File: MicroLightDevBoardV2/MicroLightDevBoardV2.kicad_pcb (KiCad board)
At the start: 2 copper layers, 88.4 x 76.5 mm, 84 parts, among them J1 Conn_01x05_Socket, J10 Conn_01x02_Socket, J11 Conn_01x05_Socket, J12 Conn_01x02_Socket, J13 Conn_01x04_Socket, J14 Conn_01x04_Socket, J15 Conn_01x05_Socket, J16 Conn_01x02_Socket, J17 Conn_01x04_Socket, J18 Conn_01x02_Socket, J19 Conn_01x02_Socket, J2 Conn_01x05_Socket, J20 Conn_01x04_Socket, J21 Conn_01x04_Socket, J22 Conn_01x02_Socket, J23 Conn_01x02_Socket, J24 Conn_01x02_Socket, J25 Conn_01x02_Socket, J26 Conn_01x02_Socket, J27 Conn_01x04_Socket, J28 Conn_01x02_Socket, J29 Conn_01x04_Socket, J3 Conn_01x05_Socket, J30 Conn_01x04_Socket, J31 Conn_01x04_Socket, J32 Conn_01x04_Socket, J33 Conn_01x04_Socket, J34 Conn_01x04_Socket, J35 Conn_01x04_Socket, J36 Conn_01x04_Socket, J37 Conn_01x04_Socket, J38 Conn_01x04_Socket, J39 Conn_01x04_Socket, J4 Conn_01x05_Socket, J40 Conn_01x04_Socket, J41 Conn_01x04_Socket, J42 Conn_01x04_Socket, J43 Conn_01x04_Socket, J44 Conn_01x04_Socket, J45 Conn_01x04_Socket, J46 Conn_01x04_Socket, J47 Conn_01x04_Socket, J48 Conn_01x04_Socket, J49 Conn_01x04_Socket, J5 Conn_01x02_Socket, J50 Conn_01x04_Socket, J6 Conn_01x02_Socket, J7 TYPE-C-31-M-12, J8 Conn_01x02_Socket, J9 Conn_01x02_Socket, U1 BQ25628RYKR, U2 ATtiny3226-M, U3 S-85S1AB33-I6T1U, U4 B3U-1000P, U5 B3U-1000P, U6 USBLC6-2P6, U7 MC3479

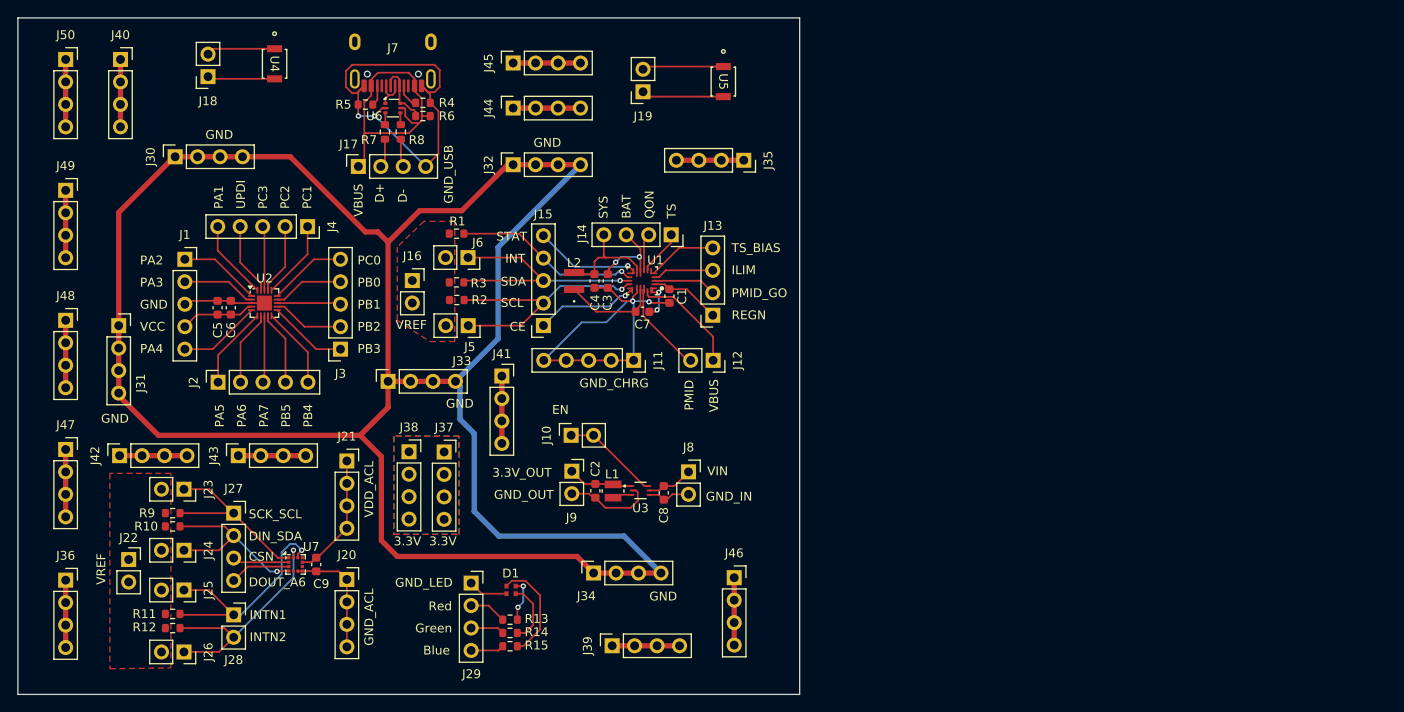
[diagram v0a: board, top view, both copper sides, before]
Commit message: organized new charger ic on pcb
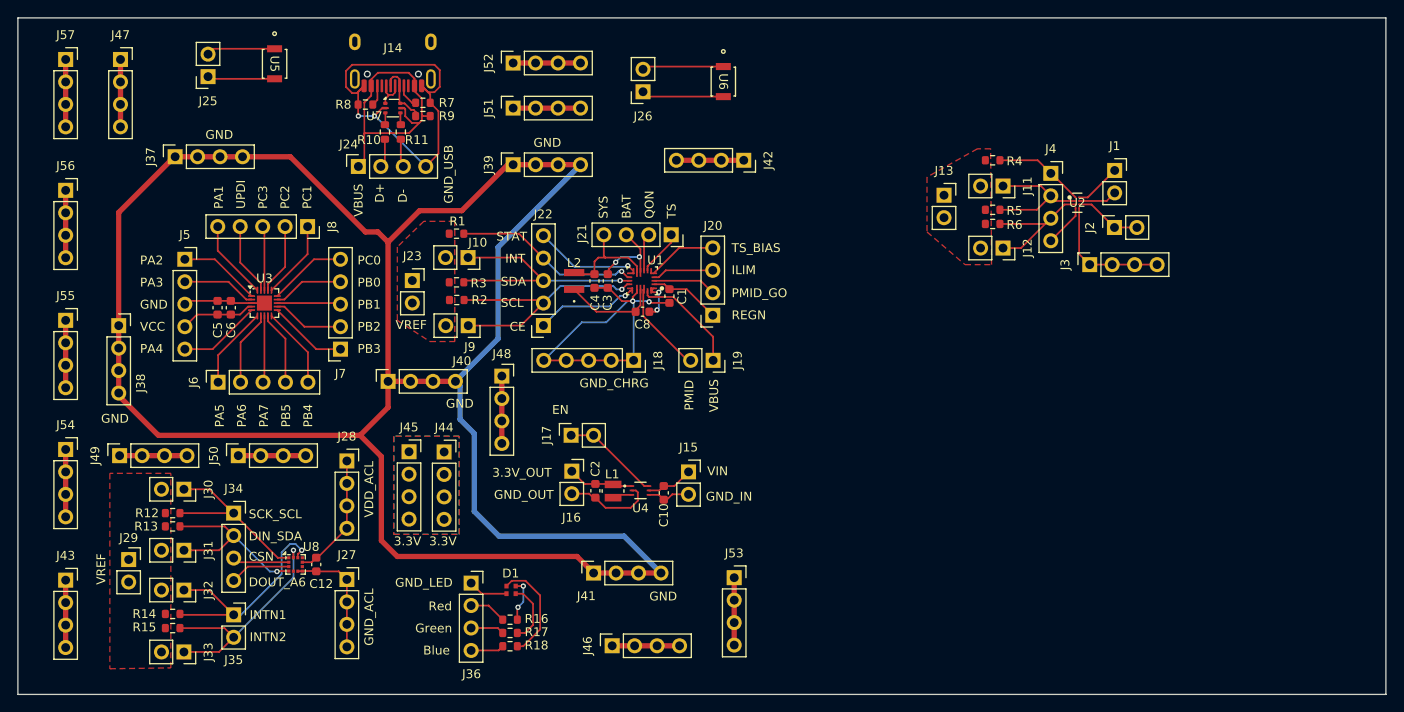
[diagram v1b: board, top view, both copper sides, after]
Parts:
- added J1: Conn_01x02_Socket, Connector_PinSocket_2.54mm:PinSocket_1x02_P2.54mm_Vertical, F.Cu at (235.3, 54.0)
- added J11: Conn_01x02_Socket, Connector_PinSocket_2.54mm:PinSocket_1x02_P2.54mm_Vertical, F.Cu at (222.7, 55.8)
- added J12: Conn_01x02_Socket, Connector_PinSocket_2.54mm:PinSocket_1x02_P2.54mm_Vertical, F.Cu at (222.7, 62.8)
- added J13: Conn_01x02_Socket, Connector_PinSocket_2.54mm:PinSocket_1x02_P2.54mm_Vertical, F.Cu at (216.0, 56.9)
- added J2: Conn_01x02_Socket, Connector_PinSocket_2.54mm:PinSocket_1x02_P2.54mm_Vertical, F.Cu at (235.3, 60.5)
- added J3: Conn_01x04_Socket, Connector_PinSocket_2.54mm:PinSocket_1x04_P2.54mm_Vertical, F.Cu at (232.5, 64.7)
- added J4: Conn_01x04_Socket, Connector_PinSocket_2.54mm:PinSocket_1x04_P2.54mm_Vertical, F.Cu at (228.1, 54.4)
- added R4: 10k, Resistor_SMD:R_0603_1608Metric, F.Cu at (221.5, 52.9)
- added R5: 10k, Resistor_SMD:R_0603_1608Metric, F.Cu at (221.5, 58.5)
- added R6: 10k, Resistor_SMD:R_0603_1608Metric, F.Cu at (221.5, 60.1)
- added U2: BQ25180, MicroLightDevBoard:BQ25180, F.Cu at (231.1, 57.7)
- renumbered C8 to C10, C9 to C12, C7 to C8, J6 to J10, J7 to J14, J8 to J15, J9 to J16, J10 to J17, J11 to J18, J12 to J19, J13 to J20, J14 to J21, J15 to J22, J16 to J23, J17 to J24, J18 to J25, J19 to J26, J20 to J27, J21 to J28, J22 to J29, J23 to J30, J24 to J31, J25 to J32, J26 to J33, J27 to J34, J28 to J35, J29 to J36, J30 to J37, J31 to J38, J32 to J39, J33 to J40, J34 to J41, J35 to J42, J36 to J43, J37 to J44, J38 to J45, J39 to J46, J40 to J47, J41 to J48, J42 to J49, J1 to J5, J43 to J50, J44 to J51, J45 to J52, J46 to J53, J47 to J54, J48 to J55, J49 to J56, J50 to J57, J2 to J6, J3 to J7, J4 to J8, J5 to J9, R7 to R10, R8 to R11, R9 to R12, R10 to R13, R11 to R14, R12 to R15, R13 to R16, R14 to R17, R15 to R18, R4 to R7, R5 to R8, R6 to R9, U2 to U3, U3 to U4, U4 to U5, U5 to U6, U6 to U7, U7 to U8
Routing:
- net SDA_CHG: track 0.00 -> 16.3 mm
- net SCL_CHG: track 0.00 -> 15.3 mm
- net GND_CHG: track 0.00 -> 14.5 mm
- net INT_CHG: track 0.00 -> 10.3 mm
- net BAT_CHG: track 0.00 -> 7.62 mm
- net VBUS_CHG: track 0.00 -> 5.29 mm
- net TS_MR_CHG: track 0.00 -> 4.86 mm
- net SYS_CHG: track 0.00 -> 4.40 mm
- added copper zone on F.Cu, net VREF_CHG
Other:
- board size 88.4 x 76.5 mm -> 154.7 x 76.5 mm

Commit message: integrated charger ic pcb breakout into the rest of the pcb
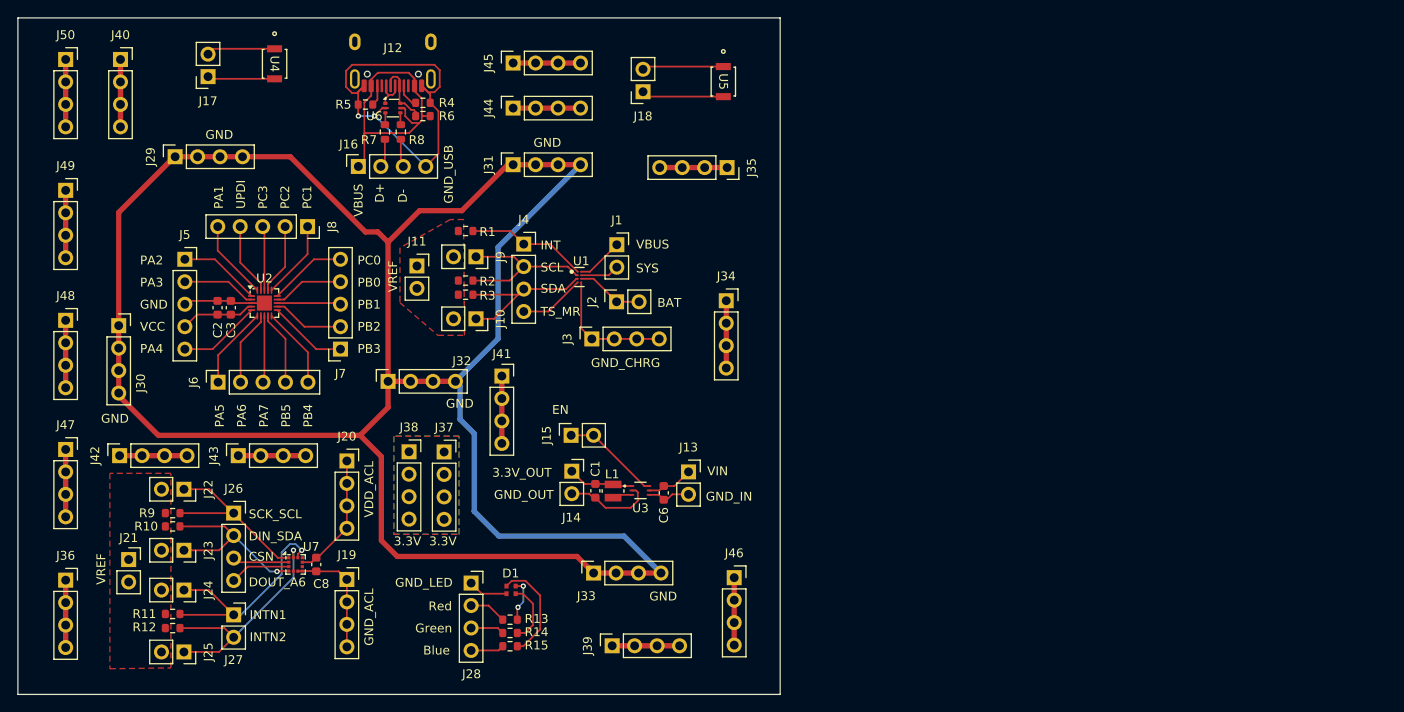
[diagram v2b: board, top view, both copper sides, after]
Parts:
- removed the C1 at (185.0, 68.2)
- removed the C3 at (178.0, 66.5)
- removed C4: 20uF, Capacitor_SMD:C_0603_1608Metric
- removed the C8 at (181.9, 70.0)
- removed the J10 at (162.2, 63.9)
- removed the J18 at (180.9, 75.5)
- removed the J19 at (189.9, 75.5)
- removed the J20 at (189.9, 70.4)
- removed the J21 at (185.2, 61.3)
- removed the J22 at (170.7, 71.6)
- removed the J23 at (155.9, 66.5)
- removed the J9 at (162.2, 71.6)
- removed L2: 1 uH, MicroLightDevBoard:74438322010_L
- removed the R1 at (160.9, 61.2)
- removed the R2 at (160.9, 68.7)
- removed the R3 at (160.9, 66.7)
- removed the U1 at (181.9, 66.5)
- added J34: Conn_01x04_Socket, Connector_PinSocket_2.54mm:PinSocket_1x04_P2.54mm_Vertical, F.Cu at (191.4, 68.8)
- moved J10 60.1 mm to (163.1, 70.8)
- moved J11 60.1 mm to (156.4, 64.8)
- moved J4 60.1 mm to (168.5, 62.4)
- moved J9 60.1 mm to (163.1, 63.8)
- moved R1 60.1 mm to (161.9, 60.9)
- moved R2 60.1 mm to (161.9, 66.5)
- moved R3 60.1 mm to (161.9, 68.1)
- moved J2 56.9 mm to (179.0, 68.9)
- moved J3 56.9 mm to (176.2, 73.1)
- moved J1 56.9 mm to (179.0, 62.4)
- moved U1 56.9 mm to (174.8, 66.1)
- moved J35 2.05 mm to (191.5, 53.7)
- renumbered C2 to C1, C5 to C2, C6 to C3, C10 to C6, C12 to C8, J12 to J10, J13 to J11, J14 to J12, J15 to J13, J16 to J14, J17 to J15, J24 to J16, J25 to J17, J26 to J18, J27 to J19, J28 to J20, J29 to J21, J30 to J22, J31 to J23, J32 to J24, J33 to J25, J34 to J26, J35 to J27, J36 to J28, J37 to J29, J38 to J30, J39 to J31, J40 to J32, J41 to J33, J42 to J35, J43 to J36, J44 to J37, J45 to J38, J46 to J39, J47 to J40, J48 to J41, J49 to J42, J50 to J43, J51 to J44, J52 to J45, J53 to J46, J54 to J47, J55 to J48, J56 to J49, J57 to J50, J11 to J9, R4 to R1, R13 to R10, R14 to R11, R15 to R12, R16 to R13, R17 to R14, R18 to R15, R5 to R2, R6 to R3, R7 to R4, R8 to R5, R9 to R6, R10 to R7, R11 to R8, R12 to R9, U2 to U1, U3 to U2, U4 to U3, U5 to U4, U6 to U5, U7 to U6, U8 to U7
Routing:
- net GND_CHRG: track 40.5 -> 0.00 mm, vias 2 -> 0
- net SCL_CHRG: track 29.6 -> 0.00 mm, vias 1 -> 0
- net SDA_CHRG: track 28.4 -> 0.00 mm, vias 1 -> 0
- net INT: track 21.1 -> 0.00 mm, vias 1 -> 0
- net SYS: track 12.7 -> 0.00 mm
- net VBUS_CHRG: track 12.5 -> 0.00 mm
- net STAT: track 11.9 -> 0.00 mm, vias 1 -> 0
- net CE: track 11.7 -> 0.00 mm, vias 1 -> 0
- net SW: track 10.8 -> 0.00 mm
- net PMID: track 10.5 -> 0.00 mm
- net BAT: track 9.63 -> 0.00 mm, vias 2 -> 0
- net REGN: track 8.06 -> 0.00 mm
- net TS_BIAS: track 7.87 -> 0.00 mm
- net Net-(J34-Pin_1): track 0.00 -> 7.62 mm
- net PMID_GO: track 7.18 -> 0.00 mm
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- removed copper zone on F.Cu, net VREF_CHRG
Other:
- board size 154.7 x 76.5 mm -> 86.2 x 76.5 mm
- board text added: "TS_MR"
- board text removed: "CE"
- board text removed: "ILIM"
- board text removed: "PMID"
- board text removed: "PMID_GO"
- board text removed: "QON"
- board text removed: "REGN"
- board text removed: "STAT"
- board text removed: "TS"
- board text removed: "TS_BIAS"

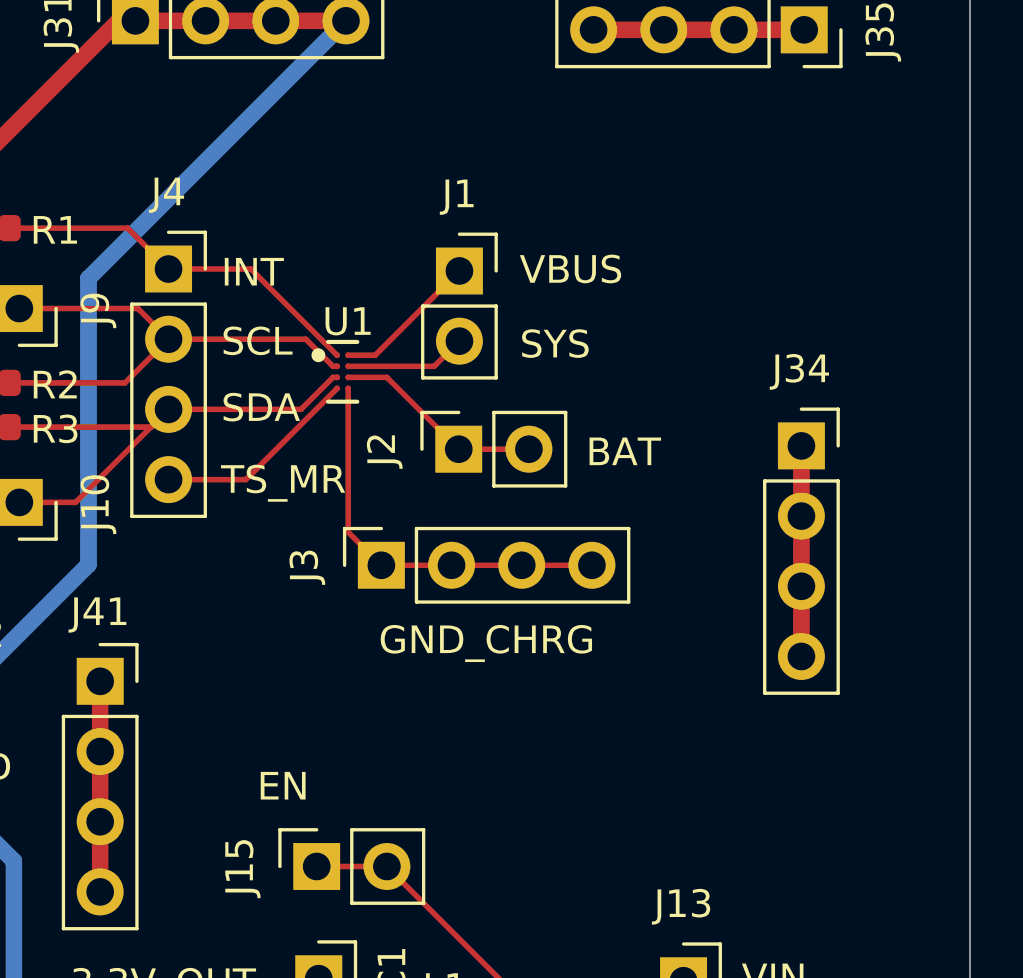
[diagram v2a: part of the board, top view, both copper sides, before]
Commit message: added missing capacitorson charging ic pcb
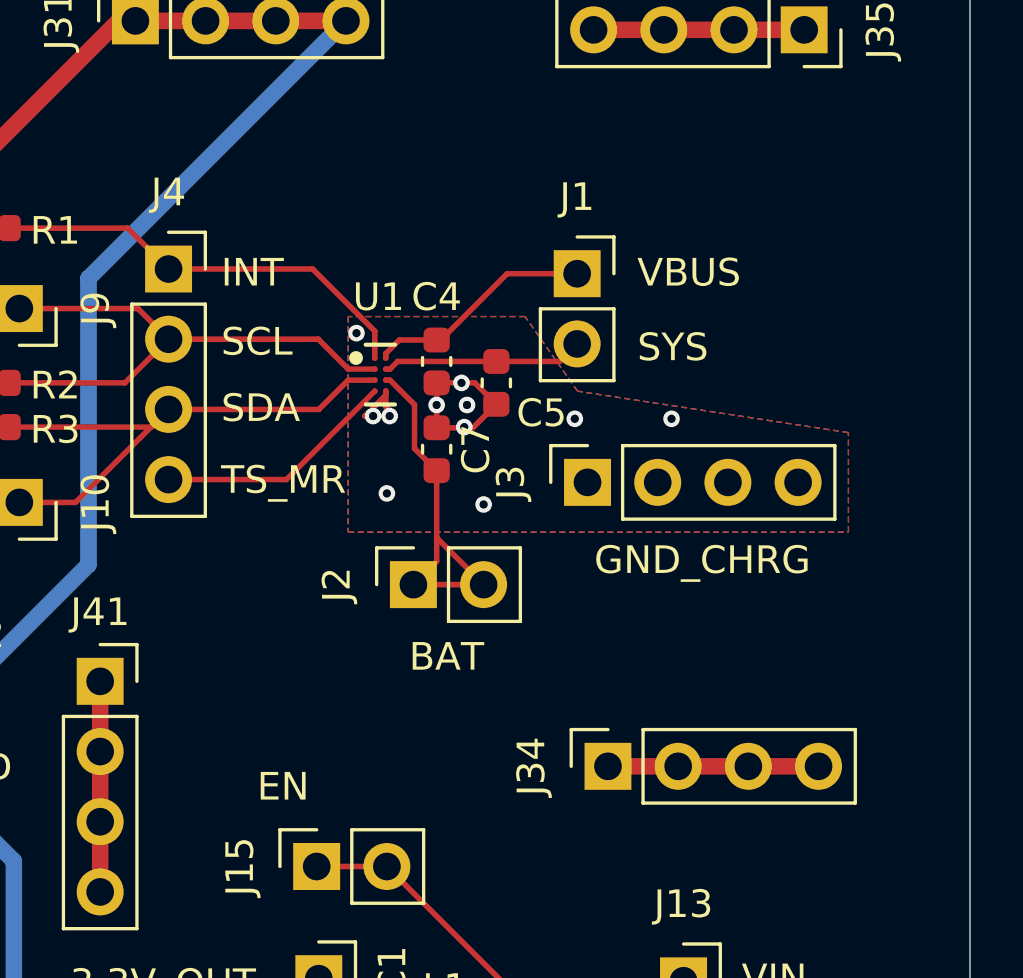
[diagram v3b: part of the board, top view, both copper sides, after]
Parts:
- added C4: C, Capacitor_SMD:C_0603_1608Metric, F.Cu at (178.2, 65.7)
- added C5: C, Capacitor_SMD:C_0603_1608Metric, F.Cu at (180.4, 66.5)
- added C7: C, Capacitor_SMD:C_0603_1608Metric, F.Cu at (178.2, 68.9)
- moved J34 13.5 mm to (184.4, 80.4), turned to 90 degrees
- moved J3 8.04 mm to (183.7, 70.1)
- moved J2 5.17 mm to (177.4, 73.8)
- moved J1 4.26 mm to (183.3, 62.5)
- moved U1 1.37 mm to (176.2, 66.2)
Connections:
- net BAT_CHG renamed BAT_CHRG
- net GND_CHG renamed GND_CHRG
- net INT_CHG renamed INT_CHRG
- net SCL_CHG renamed SCL_CHRG
- net SDA_CHG renamed SDA_CHRG
- net SYS_CHG renamed SYS_CHRG
- net TS_MR_CHG renamed TS_MR_CHRG
- net VBUS_CHG renamed VBUS_CHRG
- net VREF_CHG renamed VREF_CHRG
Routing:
- net BAT_CHRG: track 7.62 -> 13.5 mm
- net GND_CHRG: track 14.5 -> 9.45 mm, vias 0 -> 11
- net VBUS_CHRG: track 5.29 -> 8.28 mm
- net SYS_CHRG: track 4.40 -> 7.30 mm
- net INT_CHRG: track 13.8 -> 15.7 mm
- net SCL_CHRG: track 18.8 -> 20.2 mm
- net TS_MR_CHRG: track 7.47 -> 8.79 mm
- net SDA_CHRG: track 19.4 -> 20.7 mm
- added copper zone on B.Cu, net GND_CHRG
- added copper zone on F.Cu, net GND_CHRG

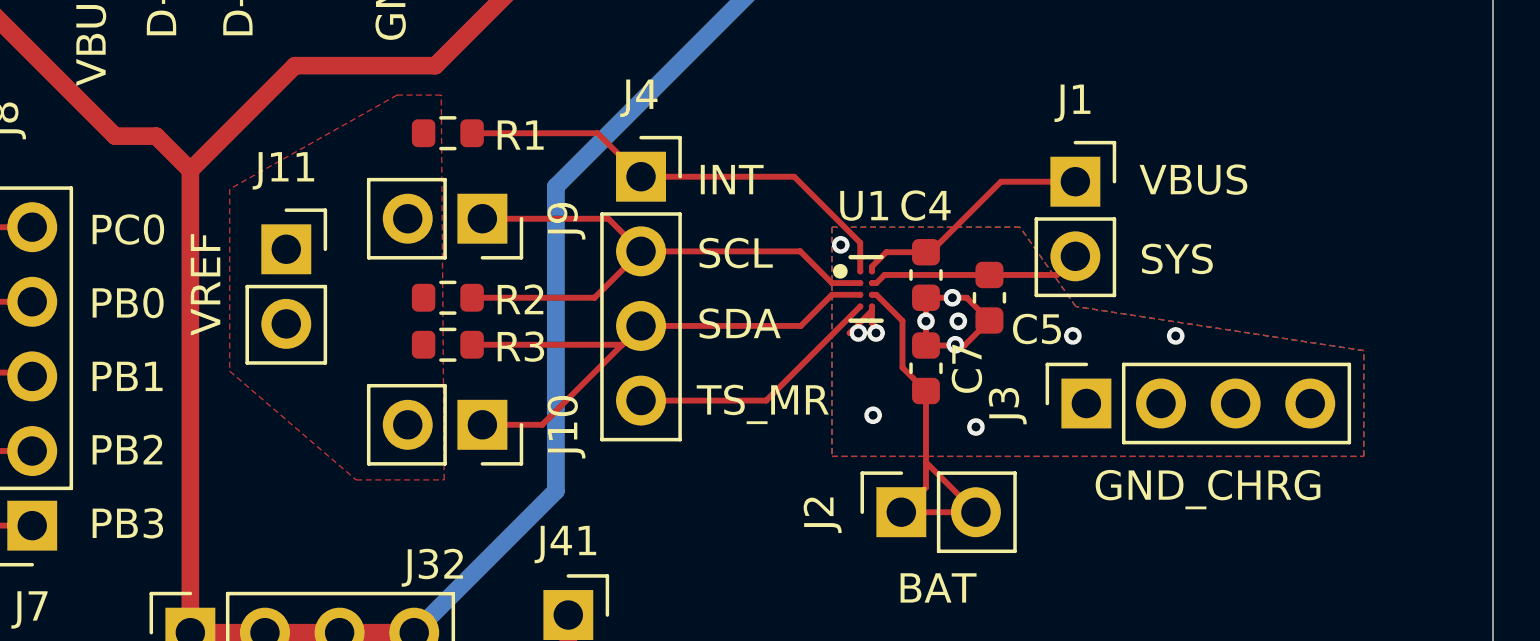
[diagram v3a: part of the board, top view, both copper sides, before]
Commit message: added capacitor values and missing resistor on TS pin of charging ic (not using TS)
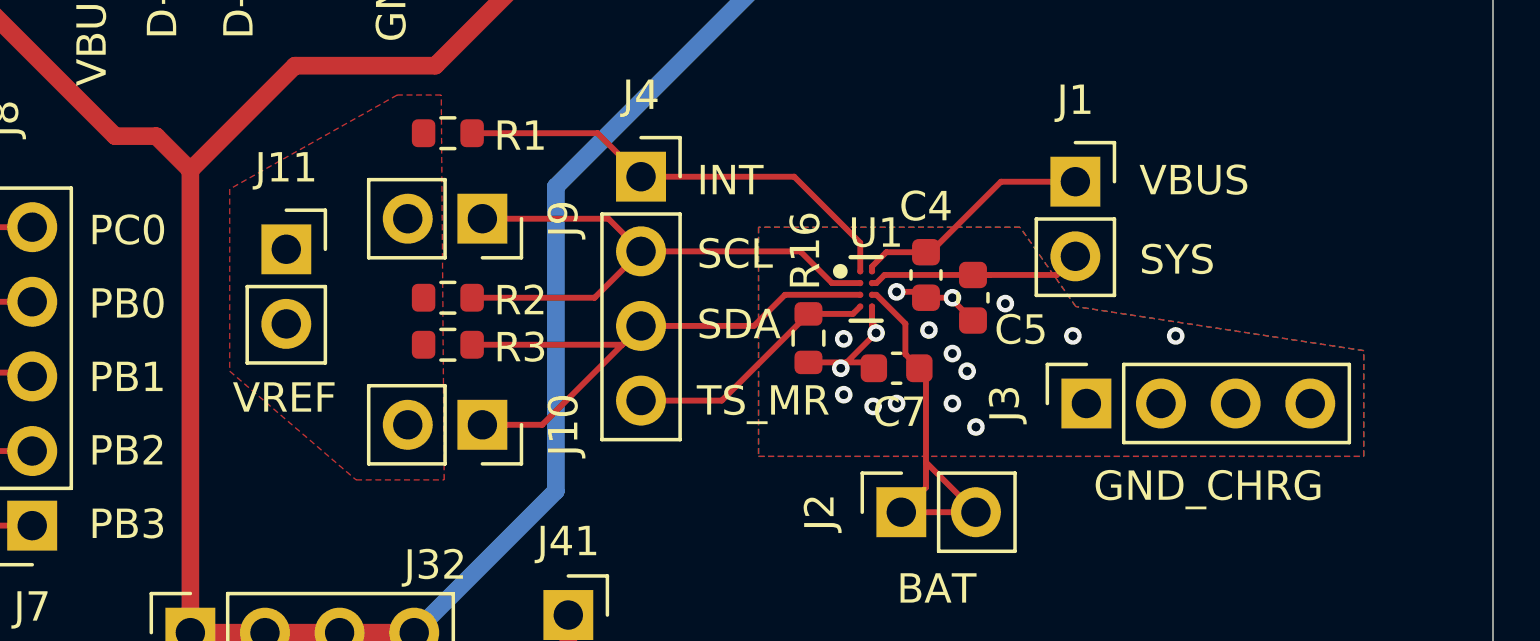
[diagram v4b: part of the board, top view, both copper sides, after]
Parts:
- added R16: 10k, Resistor_SMD:R_0603_1608Metric, F.Cu at (174.2, 67.9)
- C4, C7: value C -> 1uh 25v
- C5: value C -> 10uh
- moved C7 1.00 mm to (177.2, 68.9), turned to 0 degrees
- moved C5 0.56 mm to (179.8, 66.5)
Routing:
- net GND_CHRG: track 9.45 -> 9.15 mm, vias 11 -> 16
